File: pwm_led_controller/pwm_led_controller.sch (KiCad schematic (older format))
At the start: 79 parts, among them J1 Conn_01x06_Male, J10 Conn_01x02_Male, J11 Conn_01x02_Male, J12 Conn_01x08_Male, J2 Conn_01x09_Male, J3 Conn_01x02_Male, J4 Conn_01x08_Male, J5 Conn_01x02_Male, J6 Conn_01x02_Male, J7 Conn_01x02_Male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

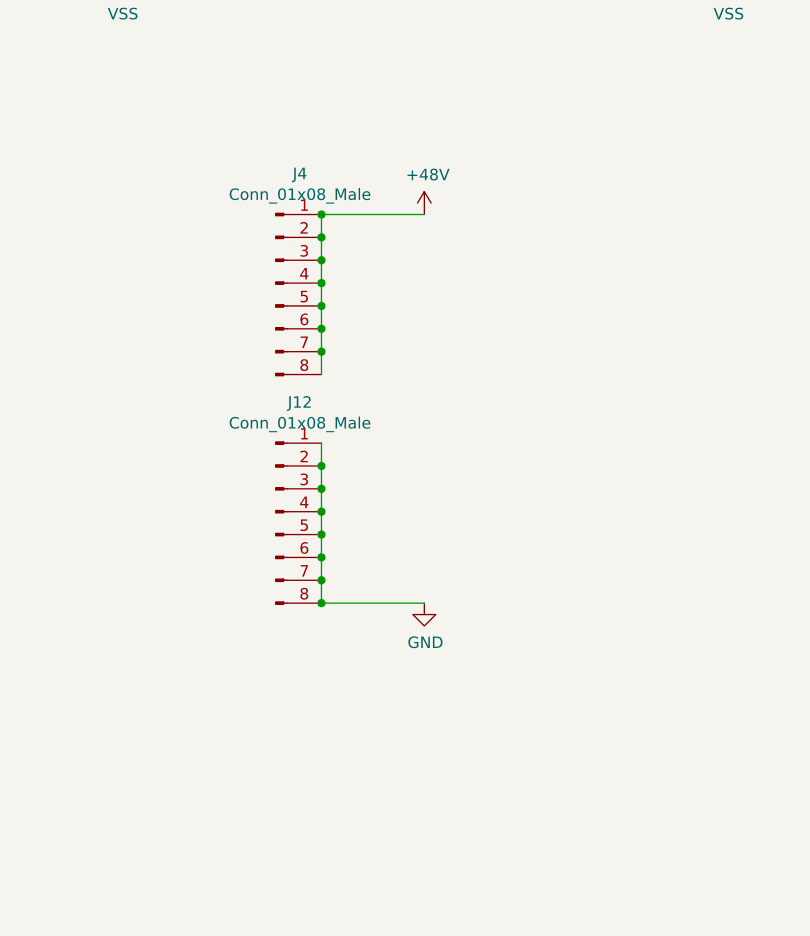
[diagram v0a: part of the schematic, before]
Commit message: Разведена силовая часть
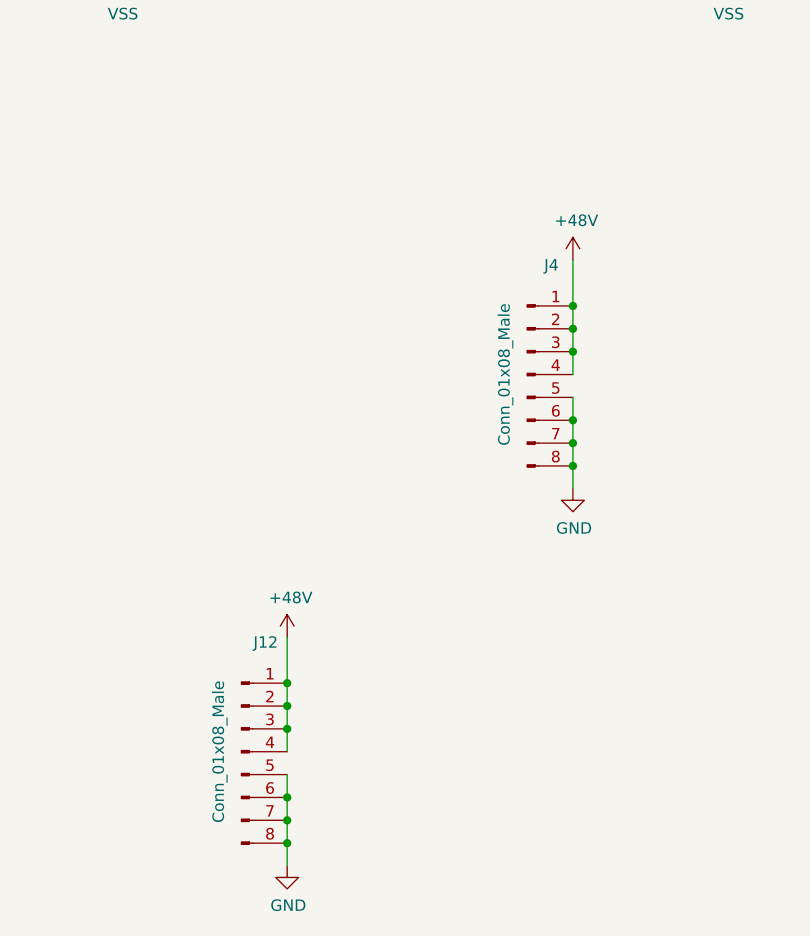
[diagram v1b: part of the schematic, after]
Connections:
- net +48V: now also J12.1 (Pin_1), J12.2 (Pin_2), J12.3 (Pin_3), J12.4 (Pin_4); no longer J4.5 (Pin_5), J4.6 (Pin_6), J4.7 (Pin_7), J4.8 (Pin_8)
- net GND: now also J4.5 (Pin_5), J4.6 (Pin_6), J4.7 (Pin_7), J4.8 (Pin_8); no longer J12.1 (Pin_1), J12.2 (Pin_2), J12.3 (Pin_3), J12.4 (Pin_4)
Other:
- moved on the sheet: J12, J4
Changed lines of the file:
@@
 L Connector:Conn_01x08_Male J4
 U 1 1 5C9A715E
-P 2100 5450
-F 0 "J4" H 2206 5928 50  0000 C CNN
-F 1 "Conn_01x08_Male" H 2206 5837 50  0000 C CNN
-F 2 "Connector_PinHeader_2.54mm:PinHeader_1x08_P2.54mm_Vertical" H 2100 5450 50  0001 C CNN
-F 3 "~" H 2100 5450 50  0001 C CNN
-	1    2100 5450
+P 3200 5850
+F 0 "J4" H 3306 6328 50  0000 C CNN
+F 1 "Conn_01x08_Male" V 3100 5850 50  0000 C CNN
+F 2 "Connector_PinHeader_2.54mm:PinHeader_1x08_P2.54mm_Vertical" H 3200 5850 50  0001 C CNN
+F 3 "~" H 3200 5850 50  0001 C CNN
+	1    3200 5850
 	1    0    0    -1
 $EndComp
@@
 L Connector:Conn_01x08_Male J12
 U 1 1 5C9A7540
-P 2100 6450
-F 0 "J12" H 2206 6928 50  0000 C CNN
-F 1 "Conn_01x08_Male" H 2206 6837 50  0000 C CNN
-F 2 "Connector_PinHeader_2.54mm:PinHeader_1x08_P2.54mm_Vertical" H 2100 6450 50  0001 C CNN
-F 3 "~" H 2100 6450 50  0001 C CNN
-	1    2100 6450
+P 1950 7500
+F 0 "J12" H 2056 7978 50  0000 C CNN
+F 1 "Conn_01x08_Male" V 1850 7500 50  0000 C CNN
+F 2 "Connector_PinHeader_2.54mm:PinHeader_1x08_P2.54mm_Vertical" H 1950 7500 50  0001 C CNN
+F 3 "~" H 1950 7500 50  0001 C CNN
+	1    1950 7500
 	1    0    0    -1
 $EndComp
@@
 L power:+48V #PWR0122
 U 1 1 5C9A77A6
-P 2750 5150
-F 0 "#PWR0122" H 2750 5000 50  0001 C CNN
-F 1 "+48V" H 2765 5323 50  0000 C CNN
-F 2 "" H 2750 5150 50  0001 C CNN
-F 3 "" H 2750 5150 50  0001 C CNN
-	1    2750 5150
+P 3400 5350
+F 0 "#PWR0122" H 3400 5200 50  0001 C CNN
+F 1 "+48V" H 3415 5523 50  0000 C CNN
+F 2 "" H 3400 5350 50  0001 C CNN
+F 3 "" H 3400 5350 50  0001 C CNN
+	1    3400 5350
+	1    0    0    -1
+$EndComp
+$Comp
+L power:GND #PWR0123
+U 1 1 5C9CC6A0
+P 3400 6350
+F 0 "#PWR0123" H 3400 6100 50  0001 C CNN
+F 1 "GND" H 3405 6177 50  0000 C CNN
+F 2 "" H 3400 6350 50  0001 C CNN
+F 3 "" H 3400 6350 50  0001 C CNN
+	1    3400 6350
 	1    0    0    -1
 $EndComp
 Wire Wire Line
-	2750 5150 2300 5150
+	3400 6350 3400 6250
+Connection ~ 3400 6050
 Wire Wire Line
-	2300 5150 2300 5250
-Connection ~ 2300 5150
-Connection ~ 2300 5250
+	3400 6050 3400 5950
+Connection ~ 3400 6150
 Wire Wire Line
-	2300 5250 2300 5350
-Connection ~ 2300 5350
+	3400 6150 3400 6050
+Connection ~ 3400 6250
 Wire Wire Line
-	2300 5350 2300 5450
-Connection ~ 2300 5450
+	3400 6250 3400 6150
 Wire Wire Line
-	2300 5450 2300 5550
-Connection ~ 2300 5550
+	3400 5350 3400 5550
+Connection ~ 3400 5550
 Wire Wire Line
-	2300 5550 2300 5650
-Connection ~ 2300 5650
+	3400 5550 3400 5650
+Connection ~ 3400 5650
 Wire Wire Line
-	2300 5650 2300 5750
-Connection ~ 2300 5750
+	3400 5650 3400 5750
+Connection ~ 3400 5750
 Wire Wire Line
-	2300 5750 2300 5850
+	3400 5750 3400 5850
 $Comp
-L power:GND #PWR0123
-U 1 1 5C9CC6A0
-P 2750 6850
-F 0 "#PWR0123" H 2750 6600 50  0001 C CNN
-F 1 "GND" H 2755 6677 50  0000 C CNN
-F 2 "" H 2750 6850 50  0001 C CNN
-F 3 "" H 2750 6850 50  0001 C CNN
-	1    2750 6850
+L power:GND #PWR?
+U 1 1 5CA12561
+P 2150 8000
+F 0 "#PWR?" H 2150 7750 50  0001 C CNN
+F 1 "GND" H 2155 7827 50  0000 C CNN
+F 2 "" H 2150 8000 50  0001 C CNN
+F 3 "" H 2150 8000 50  0001 C CNN
+	1    2150 8000
+	1    0    0    -1
+$EndComp
+$Comp
+L power:+48V #PWR?
+U 1 1 5CA12CD4
+P 2150 7000
+F 0 "#PWR?" H 2150 6850 50  0001 C CNN
+F 1 "+48V" H 2165 7173 50  0000 C CNN
+F 2 "" H 2150 7000 50  0001 C CNN
+F 3 "" H 2150 7000 50  0001 C CNN
+	1    2150 7000
 	1    0    0    -1
 $EndComp
 Wire Wire Line
-	2750 6850 2300 6850
+	2150 7000 2150 7200
+Connection ~ 2150 7200
 Wire Wire Line
-	2300 6850 2300 6750
-Connection ~ 2300 6850
-Connection ~ 2300 6250
+	2150 7200 2150 7300
+Connection ~ 2150 7300
 Wire Wire Line
-	2300 6250 2300 6150
-Connection ~ 2300 6350
+	2150 7300 2150 7400
+Connection ~ 2150 7400
 Wire Wire Line
-	2300 6350 2300 6250
-Connection ~ 2300 6450
+	2150 7400 2150 7500
 Wire Wire Line
-	2300 6450 2300 6350
-Connection ~ 2300 6550
+	2150 7600 2150 7700
+Connection ~ 2150 7700
 Wire Wire Line
-	2300 6550 2300 6450
-Connection ~ 2300 6650
+	2150 7700 2150 7800
+Connection ~ 2150 7800
 Wire Wire Line
-	2300 6650 2300 6550
-Connection ~ 2300 6750
+	2150 7800 2150 7900
+Connection ~ 2150 7900
 Wire Wire Line
-	2300 6750 2300 6650
+	2150 7900 2150 8000
 $EndSCHEMATC
